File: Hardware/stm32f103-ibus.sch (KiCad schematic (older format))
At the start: 9 parts

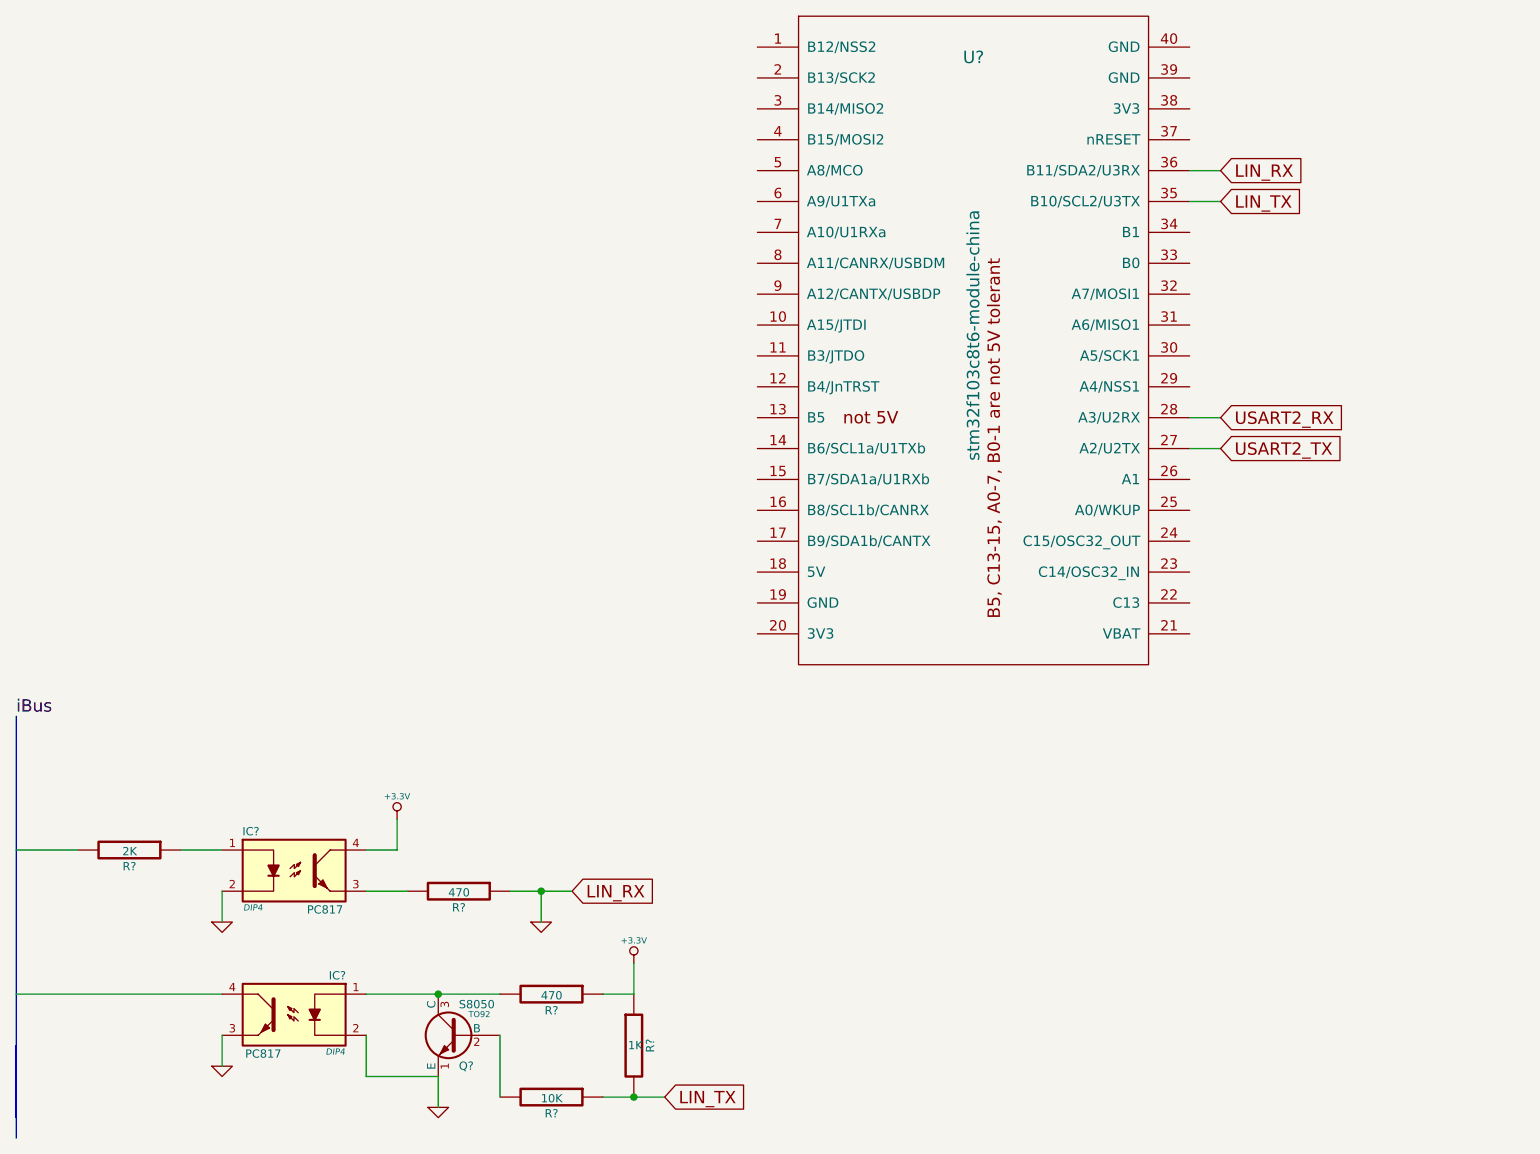
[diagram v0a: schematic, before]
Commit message: 1.Fix ibus TX/RX circuit 2.Add ADC to measure 12v voltage 3.iBus idle detect with 3 ms 4.Display water temperature / voltage on Radio screen 5.Experiment of display BC screen / IKE screen 6.Various bugs fix and testing code
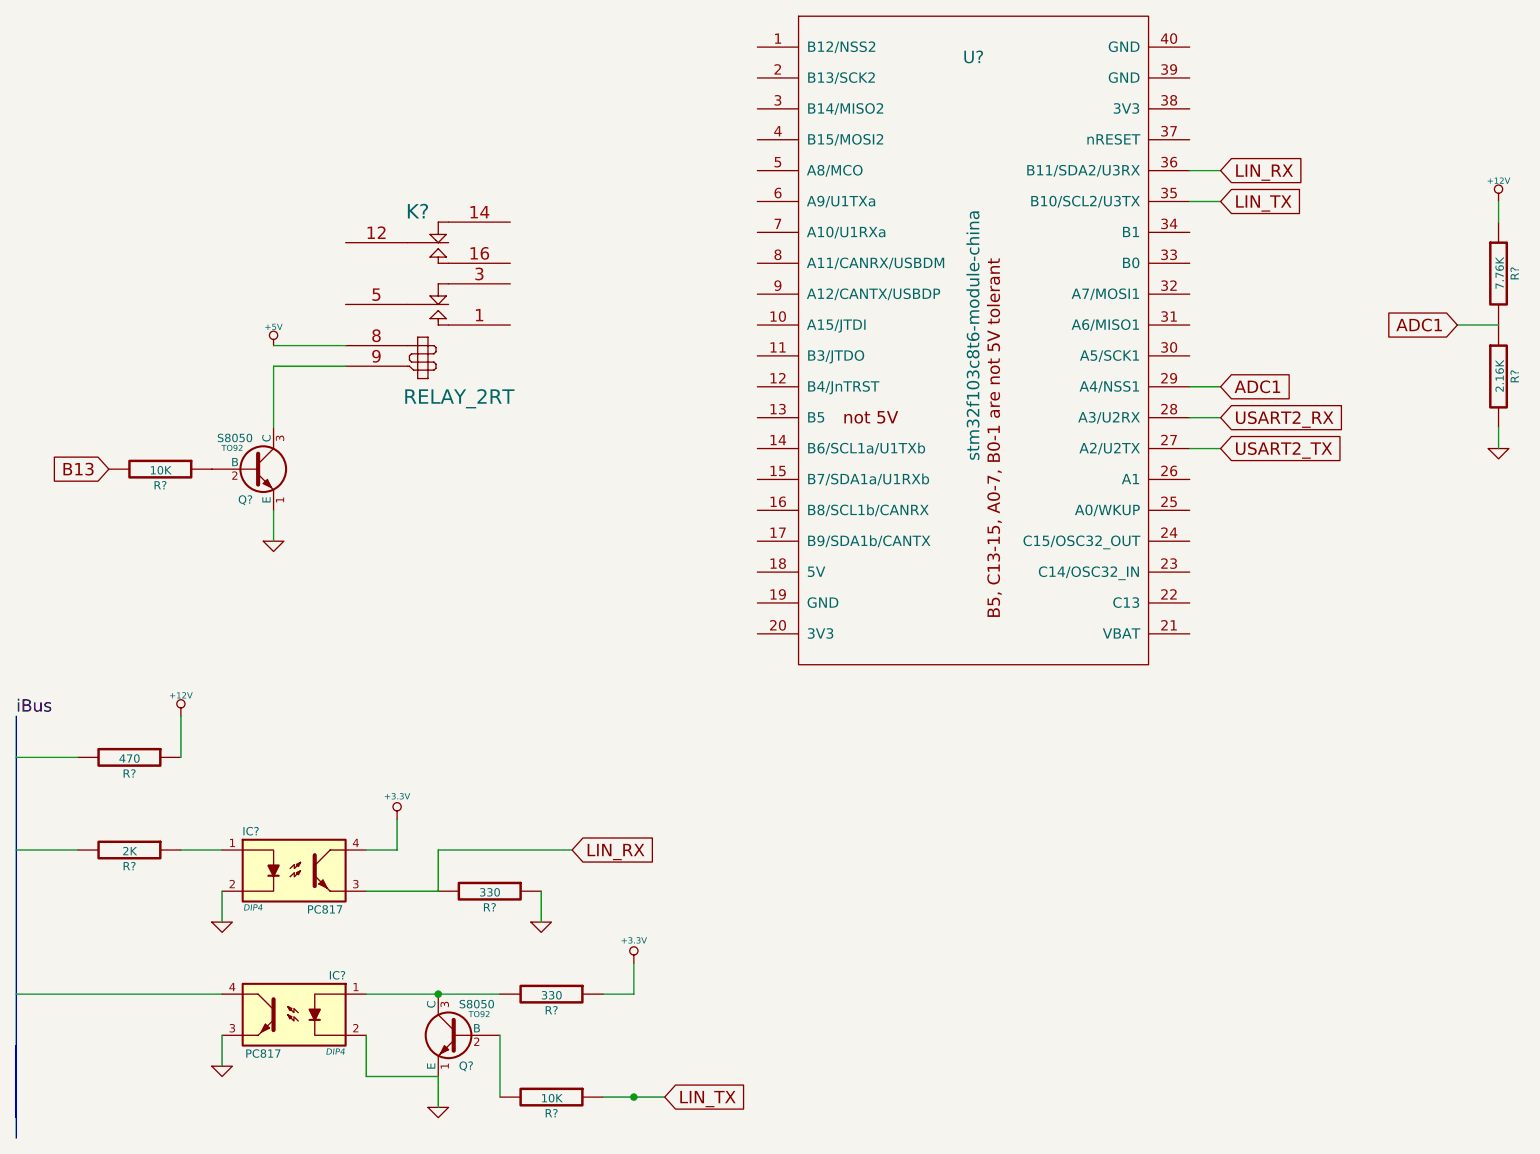
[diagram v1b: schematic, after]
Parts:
- removed R?: 1K, symbol R
- added K?: RELAY_2RT, symbol RELAY_2RT
- added Q?: S8050, TO92, symbol S8050
- added R?: 470, symbol R
- added R?: 10K, symbol R
- added R?: 7.76K, symbol R
- added R?: 2.16K, symbol R
- R? (x2): value 470 -> 330
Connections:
- net labels added: +12V, +5V, ADC1, B13
- wire segments 22 -> 33
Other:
- moved on the sheet: R?
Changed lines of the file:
@@
 L R R?
 U 1 1 595249B7
-P 2950 6150
-F 0 "R?" V 3030 6150 40  0000 C CNN
-F 1 "470" V 2957 6151 40  0000 C CNN
-F 2 "" V 2880 6150 30  0000 C CNN
-F 3 "" H 2950 6150 30  0000 C CNN
-	1    2950 6150
-	0    1    1    0
-$EndComp
-Text GLabel 3500 6150 2    60   Input ~ 0
+P 3100 6150
+F 0 "R?" V 3180 6150 40  0000 C CNN
+F 1 "330" V 3107 6151 40  0000 C CNN
+F 2 "" V 3030 6150 30  0000 C CNN
+F 3 "" H 3100 6150 30  0000 C CNN
+	1    3100 6150
+	0    1    1    0
+$EndComp
+Text GLabel 3500 5950 2    60   Input ~ 0
 LIN_RX
-$Comp
-L GND #PWR?
-U 1 1 59524A90
-P 3350 6300
-F 0 "#PWR?" H 3350 6300 30  0001 C CNN
-F 1 "GND" H 3350 6230 30  0001 C CNN
-F 2 "" H 3350 6300 60  0000 C CNN
-F 3 "" H 3350 6300 60  0000 C CNN
-	1    3350 6300
-	1    0    0    -1
-$EndComp
 $Comp
 L GND #PWR?
@@
 P 3400 6650
 F 0 "R?" V 3480 6650 40  0000 C CNN
-F 1 "470" V 3407 6651 40  0000 C CNN
+F 1 "330" V 3407 6651 40  0000 C CNN
 F 2 "" V 3330 6650 30  0000 C CNN
 F 3 "" H 3400 6650 30  0000 C CNN
@@
 	1    3400 7150
 	0    1    1    0
-$EndComp
-$Comp
-L R R?
-U 1 1 59524E64
-P 3800 6900
-F 0 "R?" V 3880 6900 40  0000 C CNN
-F 1 "1K" H 3807 6901 40  0000 C CNN
-F 2 "" V 3730 6900 30  0000 C CNN
-F 3 "" H 3800 6900 30  0000 C CNN
-	1    3800 6900
-	1    0    0    -1
 $EndComp
 $Comp
@@
 Text GLabel 3950 7150 2    60   Input ~ 0
 LIN_TX
-Wire Bus Line
-	800  5300 800  7250
-Wire Bus Line
-	800  6900 800  7350
-Wire Wire Line
-	3200 6150 3500 6150
-Wire Wire Line
-	3350 6300 3350 6150
-Connection ~ 3350 6150
-Wire Wire Line
-	2500 6150 2700 6150
-Wire Wire Line
-	800  5950 1100 5950
-Wire Wire Line
-	1600 5950 1800 5950
-Wire Wire Line
-	1800 6150 1800 6300
-Wire Wire Line
-	2500 5950 2650 5950
-Wire Wire Line
-	2650 5950 2650 5800
-Wire Wire Line
-	800  6650 1800 6650
-Wire Wire Line
-	3150 6850 3150 7150
-Wire Wire Line
-	2500 6650 3150 6650
-Connection ~ 2850 6650
-Wire Wire Line
-	3650 6650 3800 6650
-Wire Wire Line
-	3650 7150 3950 7150
-Connection ~ 3800 7150
-Wire Wire Line
-	3800 6650 3800 6500
 $Comp
 L GND #PWR?
@@
 	1    0    0    -1
 $EndComp
-Wire Wire Line
-	2850 7050 2850 7200
-Wire Wire Line
-	2500 6850 2500 7050
-Wire Wire Line
-	2500 7050 2850 7050
-Wire Wire Line
-	1800 6850 1800 7000
 Text GLabel 6650 2800 2    60   Input ~ 0
 LIN_TX
 Text GLabel 6650 2650 2    60   Input ~ 0
 LIN_RX
-Wire Wire Line
-	6500 2650 6650 2650
-Wire Wire Line
-	6500 2800 6650 2800
 Text GLabel 6650 4000 2    60   Input ~ 0
 USART2_TX
 Text GLabel 6650 3850 2    60   Input ~ 0
 USART2_RX
+$Comp
+L R R?
+U 1 1 595C74DB
+P 1350 5500
+F 0 "R?" V 1430 5500 40  0000 C CNN
+F 1 "470" V 1357 5501 40  0000 C CNN
+F 2 "" V 1280 5500 30  0000 C CNN
+F 3 "" H 1350 5500 30  0000 C CNN
+	1    1350 5500
+	0    1    1    0
+$EndComp
+$Comp
+L +12V #PWR?
+U 1 1 595C75D1
+P 1600 5300
+F 0 "#PWR?" H 1600 5250 20  0001 C CNN
+F 1 "+12V" H 1600 5400 30  0000 C CNN
+F 2 "" H 1600 5300 60  0000 C CNN
+F 3 "" H 1600 5300 60  0000 C CNN
+	1    1600 5300
+	1    0    0    -1
+$EndComp
+Wire Bus Line
+	800  5300 800  7250
+Wire Bus Line
+	800  6900 800  7350
+Wire Wire Line
+	800  5950 1100 5950
+Wire Wire Line
+	1600 5950 1800 5950
+Wire Wire Line
+	1800 6150 1800 6300
+Wire Wire Line
+	2500 5950 2650 5950
+Wire Wire Line
+	2650 5950 2650 5800
+Wire Wire Line
+	800  6650 1800 6650
+Wire Wire Line
+	3150 6850 3150 7150
+Wire Wire Line
+	2500 6650 3150 6650
+Connection ~ 2850 6650
+Wire Wire Line
+	3650 6650 3800 6650
+Wire Wire Line
+	3650 7150 3950 7150
+Connection ~ 3800 7150
+Wire Wire Line
+	3800 6650 3800 6500
+Wire Wire Line
+	2850 7050 2850 7200
+Wire Wire Line
+	2500 6850 2500 7050
+Wire Wire Line
+	2500 7050 2850 7050
+Wire Wire Line
+	1800 6850 1800 7000
+Wire Wire Line
+	6500 2650 6650 2650
+Wire Wire Line
+	6500 2800 6650 2800
 Wire Wire Line
 	6500 3850 6650 3850
 Wire Wire Line
 	6500 4000 6650 4000
+Wire Wire Line
+	1600 5300 1600 5500
+Wire Wire Line
+	800  5500 1100 5500
+$Comp
+L S8050 Q?
+U 1 1 595E1A2B
+P 1950 4100
+F 0 "Q?" H 1950 3951 40  0000 R CNN
+F 1 "S8050" H 1950 4250 40  0000 R CNN
+F 2 "TO92" H 1850 4202 29  0000 C CNN
+F 3 "" H 1950 4100 60  0000 C CNN
+	1    1950 4100
+	1    0    0    -1
+$EndComp
+Text GLabel 1250 4100 0    60   Input ~ 0
+B13
+$Comp
+L RELAY_2RT K?
+U 1 1 595E1BDB
+P 2800 3250
+F 0 "K?" H 2750 3650 70  0000 C CNN
+F 1 "RELAY_2RT" H 2950 2750 70  0000 C CNN
+F 2 "" H 2800 3250 60  0000 C CNN
+F 3 "" H 2800 3250 60  0000 C CNN
+	1    2800 3250
+	1    0    0    -1
+$EndComp
+$Comp
+L +5V #PWR?
+U 1 1 595E1CFB
+P 2050 3500
+F 0 "#PWR?" H 2050 3590 20  0001 C CNN
+F 1 "+5V" H 2050 3590 30  0000 C CNN
+F 2 "" H 2050 3500 60  0000 C CNN
+F 3 "" H 2050 3500 60  0000 C CNN
+	1    2050 3500
+	1    0    0    -1
+$EndComp
+Wire Wire Line
+	2050 3500 2400 3500
+Wire Wire Line
+	2400 3600 2050 3600
+Wire Wire Line
+	2050 3600 2050 3900
+$Comp
+L GND #PWR?
+U 1 1 595E1DC0
+P 2050 4450
+F 0 "#PWR?" H 2050 4450 30  0001 C CNN
+F 1 "GND" H 2050 4380 30  0001 C CNN
+F 2 "" H 2050 4450 60  0000 C CNN
+F 3 "" H 2050 4450 60  0000 C CNN
+	1    2050 4450
+	1    0    0    -1
+$EndComp
+Wire Wire Line
+	2050 4300 2050 4450
+$Comp
+L R R?
+U 1 1 595E2E0F
+P 1500 4100
+F 0 "R?" V 1580 4100 40  0000 C CNN
+F 1 "10K" V 1507 4101 40  0000 C CNN
+F 2 "" V 1430 4100 30  0000 C CNN
+F 3 "" H 1500 4100 30  0000 C CNN
+	1    1500 4100
+	0    1    1    0
+$EndComp
+Wire Wire Line
+	2500 6150 2850 6150
+Wire Wire Line
+	2850 6150 2850 5950
+Wire Wire Line
+	2850 5950 3500 5950
+$Comp
+L GND #PWR?
+U 1 1 596304DE
+P 3350 6300
+F 0 "#PWR?" H 3350 6300 30  0001 C CNN
+F 1 "GND" H 3350 6230 30  0001 C CNN
+F 2 "" H 3350 6300 60  0000 C CNN
+F 3 "" H 3350 6300 60  0000 C CNN
+	1    3350 6300
+	1    0    0    -1
+$EndComp
+Wire Wire Line
+	3350 6150 3350 6300
+Text GLabel 6650 3700 2    60   Input ~ 0
+ADC1
+Wire Wire Line
+	6500 3700 6650 3700
+$Comp
+L R R?
+U 1 1 5964BF5E
+P 8000 3150
+F 0 "R?" V 8080 3150 40  0000 C CNN
+F 1 "7.76K" V 8007 3151 40  0000 C CNN
+F 2 "" V 7930 3150 30  0000 C CNN
+F 3 "" H 8000 3150 30  0000 C CNN
+	1    8000 3150
+	1    0    0    -1
+$EndComp
+$Comp
+L R R?
+U 1 1 5964BF77
+P 8000 3650
+F 0 "R?" V 8080 3650 40  0000 C CNN
+F 1 "2.16K" V 8007 3651 40  0000 C CNN
+F 2 "" V 7930 3650 30  0000 C CNN
+F 3 "" H 8000 3650 30  0000 C CNN
+	1    8000 3650
+	1    0    0    -1
+$EndComp
+$Comp
+L +12V #PWR?
+U 1 1 5964C013
+P 8000 2800
+F 0 "#PWR?" H 8000 2750 20  0001 C CNN
+F 1 "+12V" H 8000 2900 30  0000 C CNN
+F 2 "" H 8000 2800 60  0000 C CNN
+F 3 "" H 8000 2800 60  0000 C CNN
+	1    8000 2800
+	1    0    0    -1
+$EndComp
+$Comp
+L GND #PWR?
+U 1 1 5964C07B
+P 8000 4000
+F 0 "#PWR?" H 8000 4000 30  0001 C CNN
+F 1 "GND" H 8000 3930 30  0001 C CNN
+F 2 "" H 8000 4000 60  0000 C CNN
+F 3 "" H 8000 4000 60  0000 C CNN
+	1    8000 4000
+	1    0    0    -1
+$EndComp
+Wire Wire Line
+	8000 2800 8000 2900
+Wire Wire Line
+	8000 3900 8000 4000
+Text GLabel 7800 3400 0    60   Input ~ 0
+ADC1
+Wire Wire Line
+	7800 3400 8000 3400
 $EndSCHEMATC

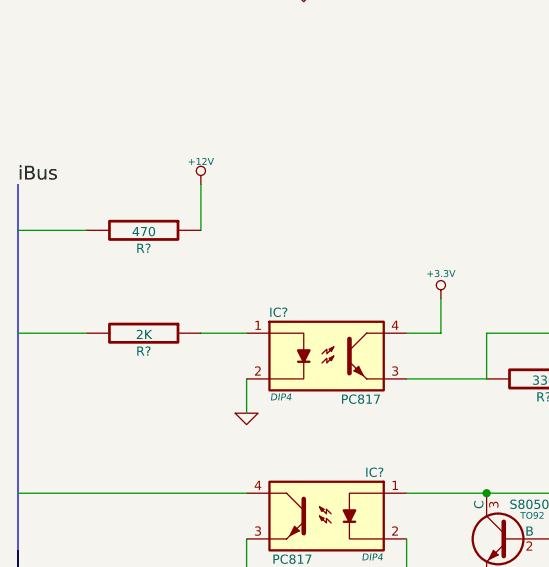
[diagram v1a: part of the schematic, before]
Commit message: 1.Add LIN transformer circuit 2.Update e38_ibus.txt 3.More IKE / Radio screen functions update
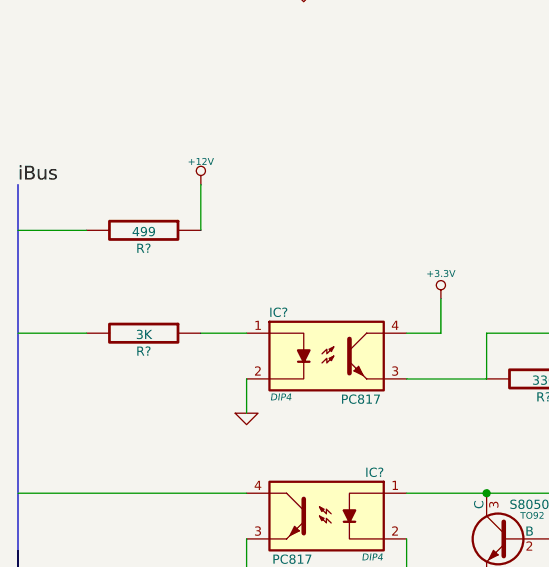
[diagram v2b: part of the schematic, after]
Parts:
- R?: value 2K -> 3K
- R?: value 470 -> 499
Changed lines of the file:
@@
 P 1350 5950
 F 0 "R?" V 1430 5950 40  0000 C CNN
-F 1 "2K" V 1357 5951 40  0000 C CNN
+F 1 "3K" V 1357 5951 40  0000 C CNN
 F 2 "" V 1280 5950 30  0000 C CNN
 F 3 "" H 1350 5950 30  0000 C CNN
@@
 P 1350 5500
 F 0 "R?" V 1430 5500 40  0000 C CNN
-F 1 "470" V 1357 5501 40  0000 C CNN
+F 1 "499" V 1357 5501 40  0000 C CNN
 F 2 "" V 1280 5500 30  0000 C CNN
 F 3 "" H 1350 5500 30  0000 C CNN
